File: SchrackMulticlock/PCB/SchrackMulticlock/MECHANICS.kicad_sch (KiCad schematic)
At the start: 34 parts, among them SW2 SW_Push, SW3 SW_Push, SW4 SW_Push, SW5 SW_Push, SW6 SW_Push, SW7 SW_Push, SW8 SW_Push, SW9 SW_Push, U8 74HC14

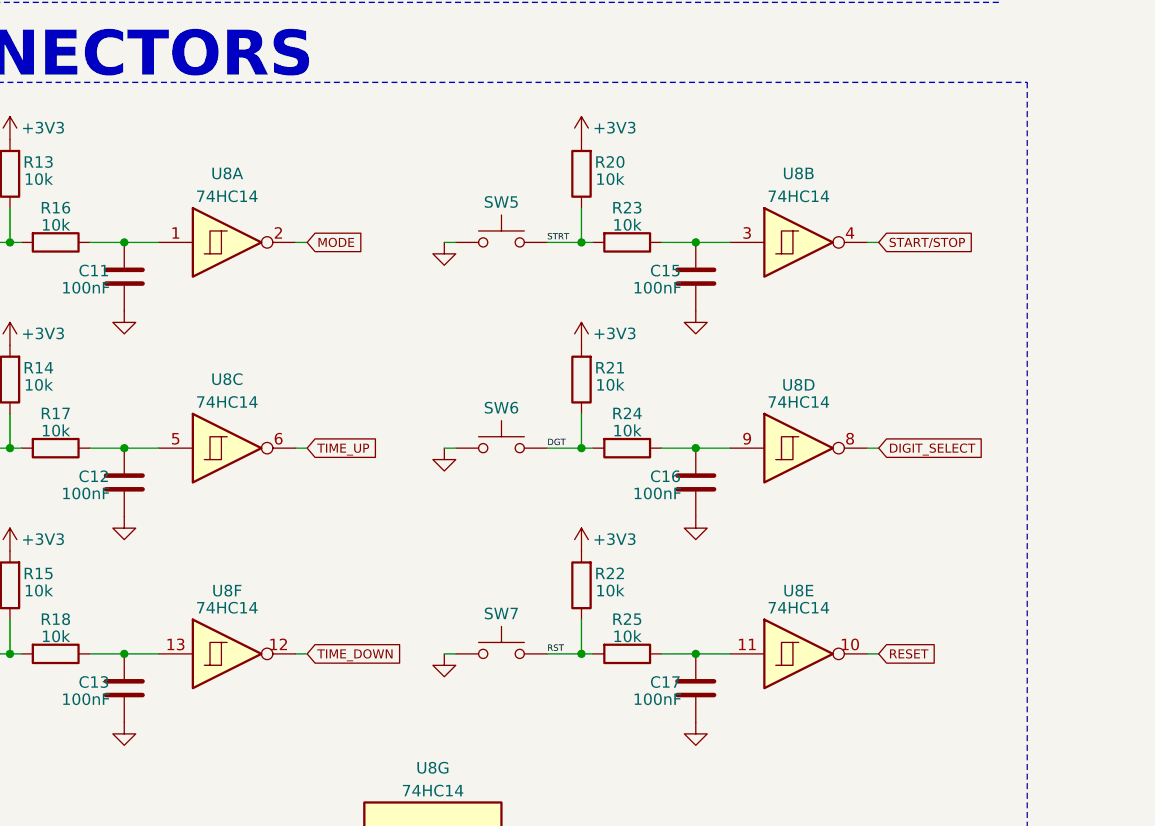
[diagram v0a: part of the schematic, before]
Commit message: Multiclock a lot of routing and layout
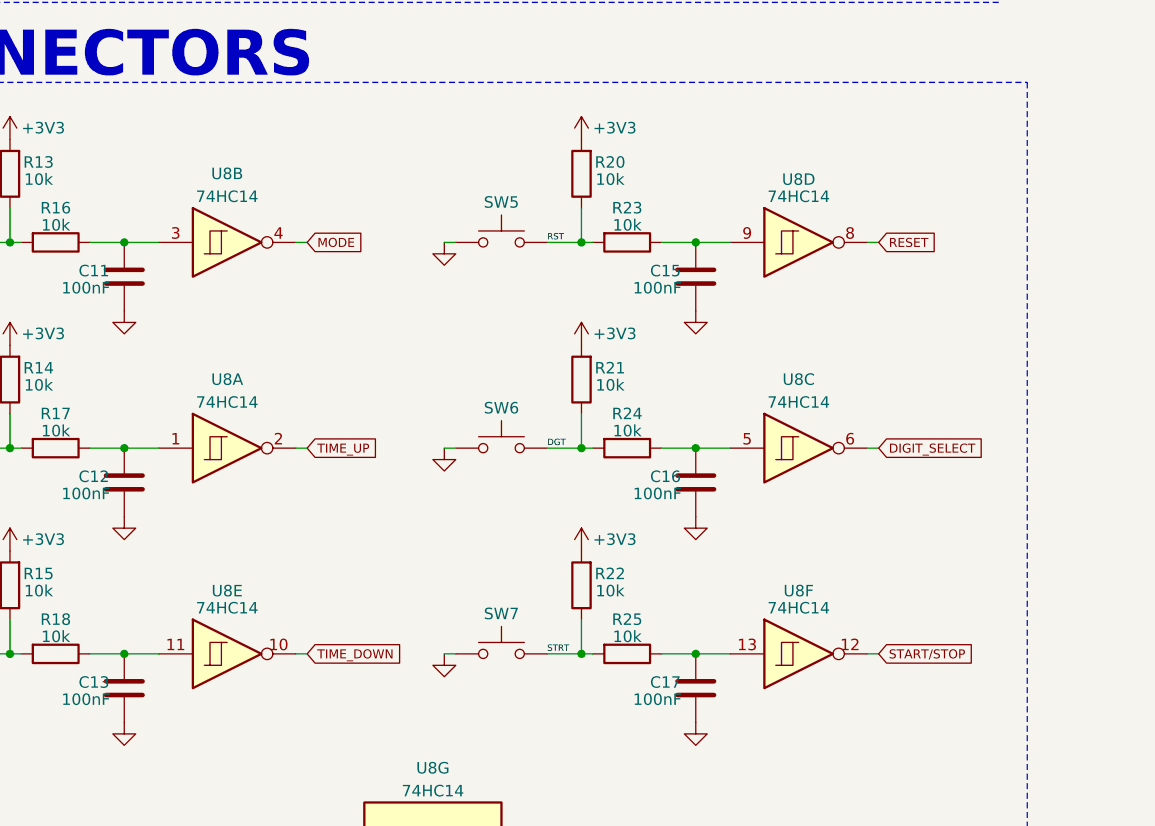
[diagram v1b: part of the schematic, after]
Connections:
- net DIGIT_SELECT: now also U8.6; no longer U8.8
- net MODE: now also U8.4; no longer U8.2
- net RESET: now also U8.8; no longer U8.10
- net RST: now also R20.1, R23.2, SW5.2; no longer R22.1, R25.2, SW7.2
- net START/STOP: now also U8.12; no longer U8.4
- net STRT: now also R22.1, R25.2, SW7.2; no longer R20.1, R23.2, SW5.2
- net TIME_DOWN: now also U8.10; no longer U8.12
- net TIME_UP: now also U8.2; no longer U8.6
- net at C15.2, R23.1: now also U8.9; no longer U8.3
- net at C16.2, R24.1: now also U8.5; no longer U8.9
- net at C13.2, R18.1: now also U8.11; no longer U8.13
- net at C17.2, R25.1: now also U8.13; no longer U8.11
- net at C12.2, R17.1: now also U8.1; no longer U8.5
- net at C11.2, R16.1: now also U8.3; no longer U8.1

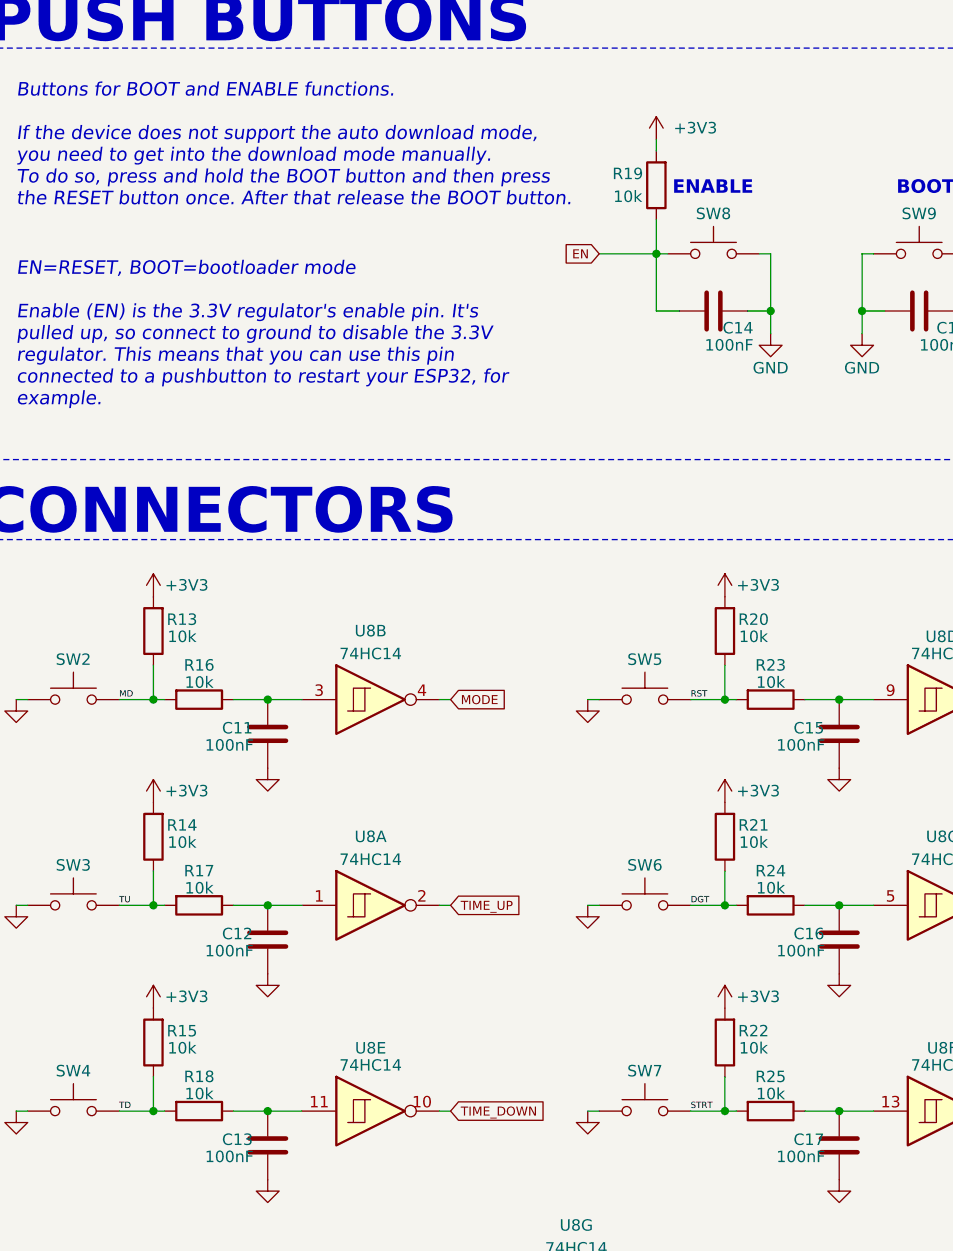
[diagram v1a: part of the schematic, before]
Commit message: Multiclock silkscreen updafe
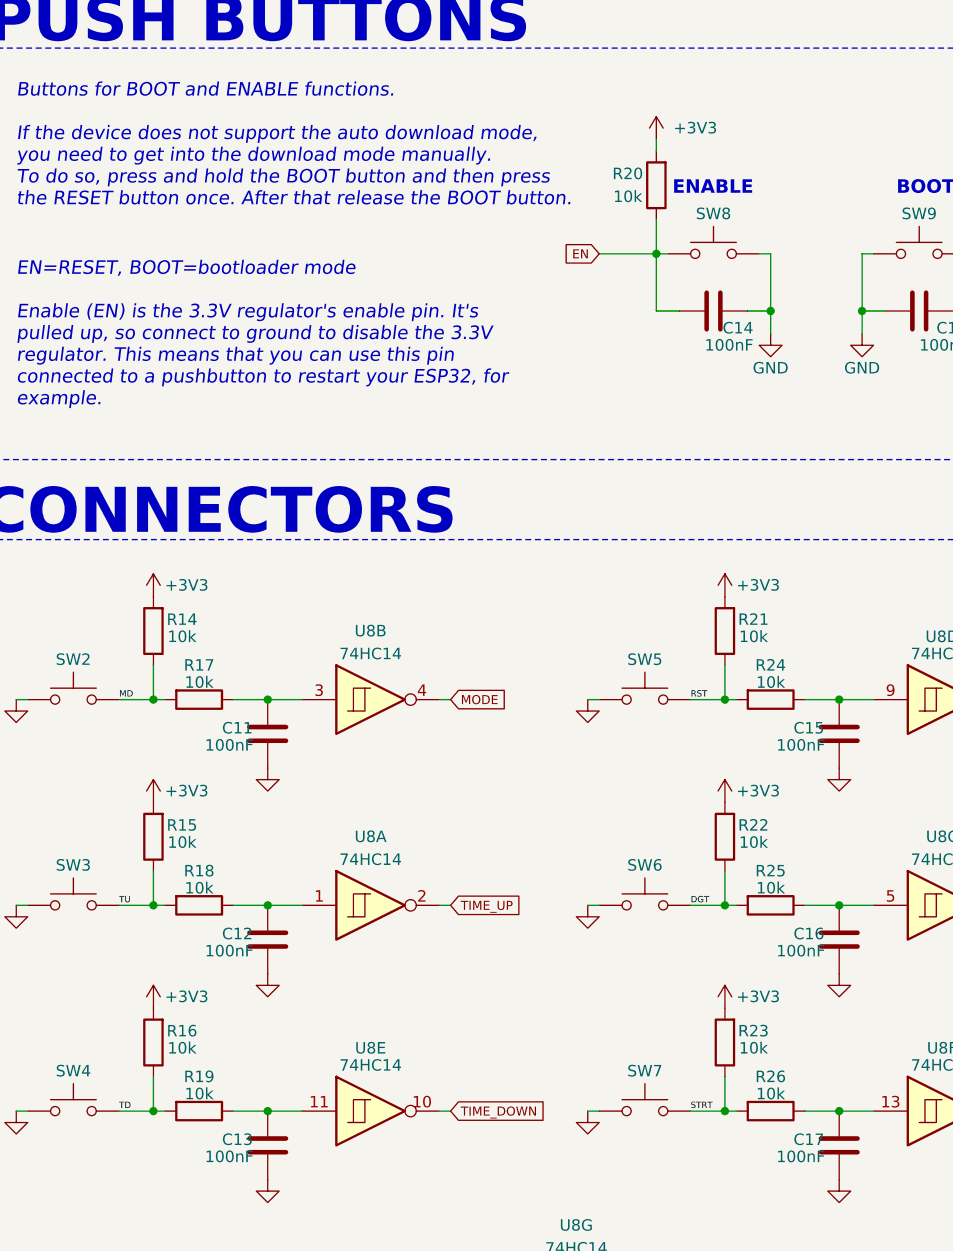
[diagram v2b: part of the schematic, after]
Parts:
- renumbered R13 to R14, R14 to R15, R15 to R16, R16 to R17, R17 to R18, R18 to R19, R19 to R20, R20 to R21, R21 to R22, R22 to R23, R23 to R24, R24 to R25, R25 to R26
